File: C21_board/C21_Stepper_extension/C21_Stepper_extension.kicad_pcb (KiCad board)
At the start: 2 copper layers, 65.8 x 36.2 mm, 22 parts, among them J1 Conn_01x04_Male, J10 Conn_01x02_Male, J11 Conn_01x02_Male, J12 Conn_01x04_Male, J2 Conn_01x02_Male, J3 Conn_01x02_Male, J4 Conn_01x02_Male, J5 Jack-DC, J6 Screw_Terminal_01x02, J7 Conn_01x04_Male, J8 Conn_01x02_Male, J9 Conn_01x04_Male

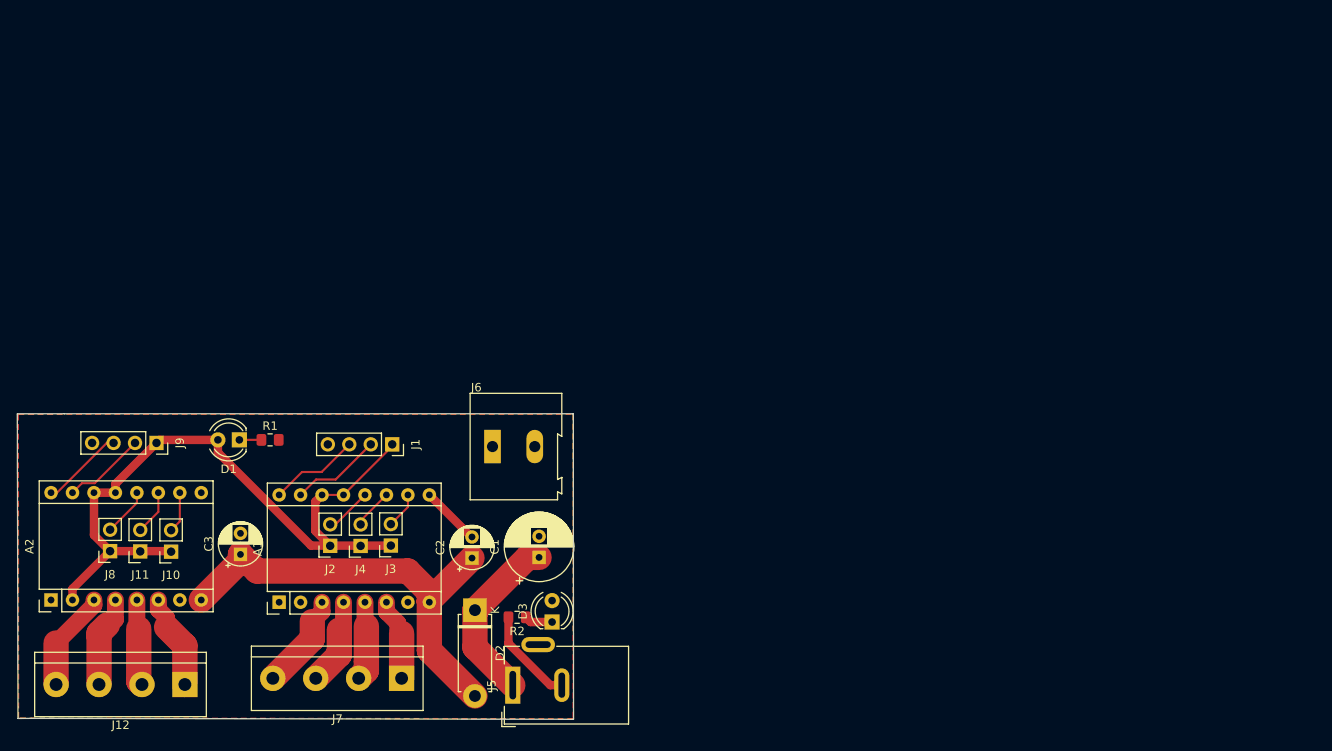
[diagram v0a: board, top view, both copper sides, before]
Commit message: add robot arm
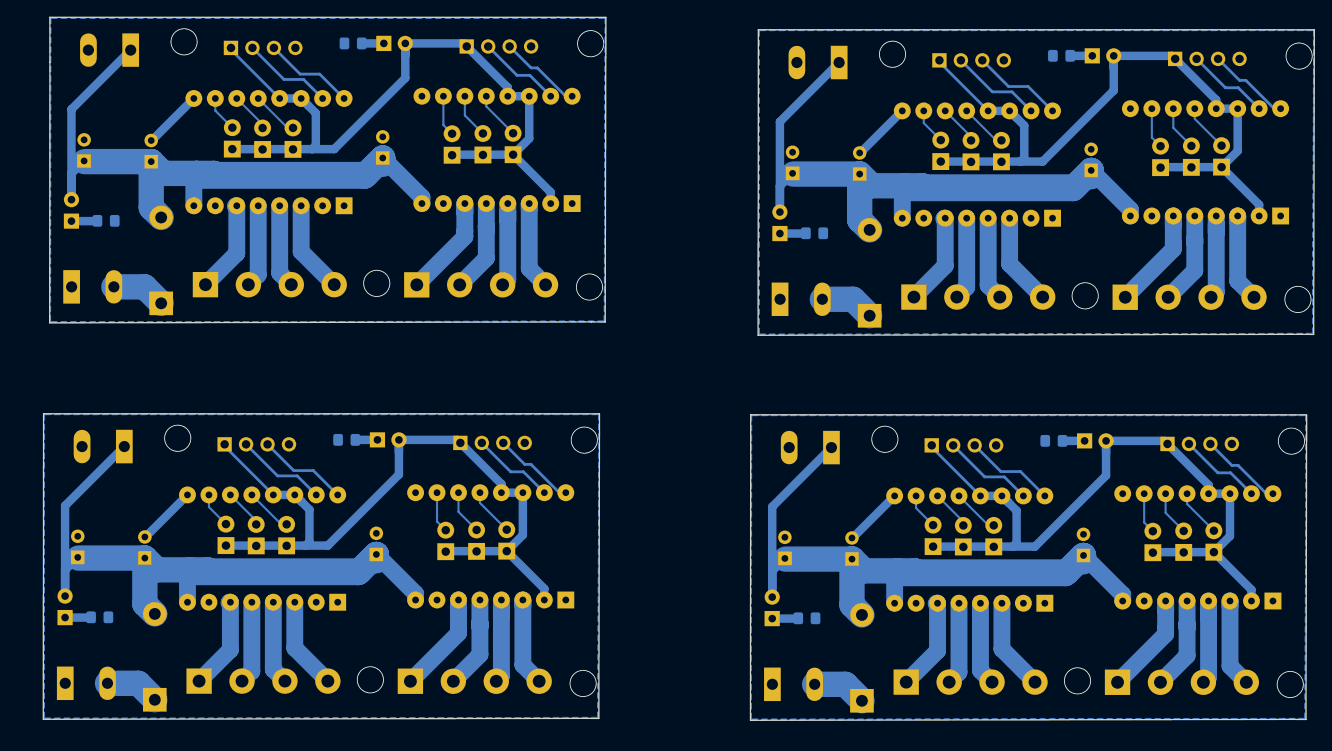
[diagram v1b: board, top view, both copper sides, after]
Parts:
- removed the J5 at (150.4, 103.6)
- added A1: Pololu_Breakout_DRV8825, drone_v3:Pololu_Breakout-16_15.2x20.3mm, B.Cu at (214.3, 48.4)
- added A1: Pololu_Breakout_DRV8825, drone_v3:Pololu_Breakout-16_15.2x20.3mm, B.Cu at (130.4, 46.9)
- added A1: Pololu_Breakout_DRV8825, drone_v3:Pololu_Breakout-16_15.2x20.3mm, B.Cu at (213.3, 93.9)
- added A2: Pololu_Breakout_DRV8825, Module:Pololu_Breakout-16_15.2x20.3mm, B.Cu at (240.3, 93.7)
- added A2: Pololu_Breakout_DRV8825, Module:Pololu_Breakout-16_15.2x20.3mm, B.Cu at (157.4, 46.6)
- added A2: Pololu_Breakout_DRV8825, Module:Pololu_Breakout-16_15.2x20.3mm, B.Cu at (241.3, 48.1)
- added C1: CP, Capacitor_THT:CP_Radial_D8.0mm_P2.50mm, B.Cu at (182.6, 88.6)
- added C1: CP, Capacitor_THT:CP_Radial_D8.0mm_P2.50mm, B.Cu at (183.5, 43.1)
- added C1: CP, Capacitor_THT:CP_Radial_D8.0mm_P2.50mm, B.Cu at (99.6, 41.6)
- added C2: CP, Capacitor_THT:CP_Radial_D5.0mm_P2.50mm, B.Cu at (190.5, 88.7)
- added C2: CP, Capacitor_THT:CP_Radial_D5.0mm_P2.50mm, B.Cu at (191.4, 43.1)
- added C2: CP, Capacitor_THT:CP_Radial_D5.0mm_P2.50mm, B.Cu at (107.6, 41.7)
- added C3: CP, Capacitor_THT:CP_Radial_D5.0mm_P2.50mm, B.Cu at (135.0, 41.2)
- added C3: CP, Capacitor_THT:CP_Radial_D5.0mm_P2.50mm, B.Cu at (217.9, 88.3)
- added C3: CP, Capacitor_THT:CP_Radial_D5.0mm_P2.50mm, B.Cu at (218.8, 42.7)
- added D1: LED, LED_THT:LED_D4.0mm, B.Cu at (135.1, 27.7)
- added D1: LED, LED_THT:LED_D4.0mm, B.Cu at (218.1, 74.7)
- added D1: LED, LED_THT:LED_D4.0mm, B.Cu at (219.0, 29.2)
- added D2: DIODE, Diode_THT:D_5W_P10.16mm_Horizontal, B.Cu at (191.7, 105.5)
- added D2: DIODE, Diode_THT:D_5W_P10.16mm_Horizontal, B.Cu at (108.8, 58.5)
- added D2: DIODE, Diode_THT:D_5W_P10.16mm_Horizontal, B.Cu at (192.6, 59.9)
- added D3: LED, LED_THT:LED_D4.0mm, B.Cu at (182.0, 50.2)
- added D3: LED, LED_THT:LED_D4.0mm, B.Cu at (98.1, 48.7)
- added D3: LED, LED_THT:LED_D4.0mm, B.Cu at (181.1, 95.8)
- added J1: Conn_01x04_Male, Connector_PinSocket_2.54mm:PinSocket_1x04_P2.54mm_Vertical, B.Cu at (200.0, 75.3)
- added J1: Conn_01x04_Male, Connector_PinSocket_2.54mm:PinSocket_1x04_P2.54mm_Vertical, B.Cu at (117.0, 28.2)
- added J1: Conn_01x04_Male, Connector_PinSocket_2.54mm:PinSocket_1x04_P2.54mm_Vertical, B.Cu at (200.9, 29.7)
- added J10: Conn_01x02_Male, drone_v3:PinSocket_1x02_P2.54mm_Vertical, B.Cu at (143.2, 40.9)
- added J10: Conn_01x02_Male, drone_v3:PinSocket_1x02_P2.54mm_Vertical, B.Cu at (226.1, 88.0)
- added J10: Conn_01x02_Male, drone_v3:PinSocket_1x02_P2.54mm_Vertical, B.Cu at (227.0, 42.4)
- added J11: Conn_01x02_Male, drone_v3:PinSocket_1x02_P2.54mm_Vertical, B.Cu at (146.8, 40.9)
- added J11: Conn_01x02_Male, drone_v3:PinSocket_1x02_P2.54mm_Vertical, B.Cu at (230.7, 42.4)
- added J11: Conn_01x02_Male, drone_v3:PinSocket_1x02_P2.54mm_Vertical, B.Cu at (229.8, 87.9)
- added J12: Conn_01x04_Male, TerminalBlock:TerminalBlock_bornier-4_P5.08mm, B.Cu at (222.9, 57.7)
- added J12: Conn_01x04_Male, TerminalBlock:TerminalBlock_bornier-4_P5.08mm, B.Cu at (139.0, 56.3)
- added J12: Conn_01x04_Male, TerminalBlock:TerminalBlock_bornier-4_P5.08mm, B.Cu at (222.0, 103.3)
- added J2: Conn_01x02_Male, Connector_PinSocket_2.54mm:PinSocket_1x02_P2.54mm_Vertical, B.Cu at (208.2, 41.7)
- added J2: Conn_01x02_Male, Connector_PinSocket_2.54mm:PinSocket_1x02_P2.54mm_Vertical, B.Cu at (207.3, 87.3)
- added J2: Conn_01x02_Male, Connector_PinSocket_2.54mm:PinSocket_1x02_P2.54mm_Vertical, B.Cu at (124.4, 40.2)
- added J3: Conn_01x02_Male, drone_v3:PinSocket_1x02_P2.54mm_Vertical, B.Cu at (201.0, 41.7)
- added J3: Conn_01x02_Male, drone_v3:PinSocket_1x02_P2.54mm_Vertical, B.Cu at (200.1, 87.2)
- added J3: Conn_01x02_Male, drone_v3:PinSocket_1x02_P2.54mm_Vertical, B.Cu at (117.2, 40.2)
- added J4: Conn_01x02_Male, drone_v3:PinSocket_1x02_P2.54mm_Vertical, B.Cu at (203.7, 87.3)
- added J4: Conn_01x02_Male, drone_v3:PinSocket_1x02_P2.54mm_Vertical, B.Cu at (204.6, 41.7)
- added J4: Conn_01x02_Male, drone_v3:PinSocket_1x02_P2.54mm_Vertical, B.Cu at (120.8, 40.2)
- added J5: Screw_Terminal_01x02, TerminalBlock:TerminalBlock_Altech_AK300-2_P5.00mm, B.Cu at (97.4, 103.4)
- added J5: Screw_Terminal_01x02, TerminalBlock:TerminalBlock_Altech_AK300-2_P5.00mm, B.Cu at (182.0, 58.0)
- added J5: Screw_Terminal_01x02, TerminalBlock:TerminalBlock_Altech_AK300-2_P5.00mm, B.Cu at (181.1, 103.5)
- added J5: Screw_Terminal_01x02, TerminalBlock:TerminalBlock_Altech_AK300-2_P5.00mm, B.Cu at (98.2, 56.5)
- added J6: Screw_Terminal_01x02, TerminalBlock:TerminalBlock_Altech_AK300-2_P5.00mm, B.Cu at (189.0, 29.9)
- added J6: Screw_Terminal_01x02, TerminalBlock:TerminalBlock_Altech_AK300-2_P5.00mm, B.Cu at (188.1, 75.5)
- added J6: Screw_Terminal_01x02, TerminalBlock:TerminalBlock_Altech_AK300-2_P5.00mm, B.Cu at (105.2, 28.5)
- added J7: Conn_01x04_Male, TerminalBlock:TerminalBlock_bornier-4_P5.08mm, B.Cu at (197.9, 57.7)
- added J7: Conn_01x04_Male, TerminalBlock:TerminalBlock_bornier-4_P5.08mm, B.Cu at (114.0, 56.2)
- added J7: Conn_01x04_Male, TerminalBlock:TerminalBlock_bornier-4_P5.08mm, B.Cu at (196.9, 103.3)
- added J8: Conn_01x02_Male, drone_v3:PinSocket_1x02_P2.54mm_Vertical, B.Cu at (150.4, 40.9)
- added J8: Conn_01x02_Male, drone_v3:PinSocket_1x02_P2.54mm_Vertical, B.Cu at (234.3, 42.3)
- added J8: Conn_01x02_Male, drone_v3:PinSocket_1x02_P2.54mm_Vertical, B.Cu at (233.4, 87.9)
- added J9: Conn_01x04_Male, Connector_PinSocket_2.54mm:PinSocket_1x04_P2.54mm_Vertical, B.Cu at (227.9, 75.1)
- added J9: Conn_01x04_Male, Connector_PinSocket_2.54mm:PinSocket_1x04_P2.54mm_Vertical, B.Cu at (228.8, 29.5)
- added J9: Conn_01x04_Male, Connector_PinSocket_2.54mm:PinSocket_1x04_P2.54mm_Vertical, B.Cu at (144.9, 28.1)
- added R1: R, Resistor_SMD:R_0805_2012Metric_Pad1.15x1.40mm_HandSolder, B.Cu at (131.5, 27.7)
- added R1: R, Resistor_SMD:R_0805_2012Metric_Pad1.15x1.40mm_HandSolder, B.Cu at (215.3, 29.2)
- added R1: R, Resistor_SMD:R_0805_2012Metric_Pad1.15x1.40mm_HandSolder, B.Cu at (214.4, 74.7)
- added R2: R, Resistor_SMD:R_0805_2012Metric_Pad1.15x1.40mm_HandSolder, B.Cu at (102.2, 48.7)
- added R2: R, Resistor_SMD:R_0805_2012Metric_Pad1.15x1.40mm_HandSolder, B.Cu at (185.2, 95.7)
- added R2: R, Resistor_SMD:R_0805_2012Metric_Pad1.15x1.40mm_HandSolder, B.Cu at (186.1, 50.2)
- A1: footprint Module:Pololu_Breakout-16_15.2x20.3mm -> drone_v3:Pololu_Breakout-16_15.2x20.3mm; moved to B.Cu
- A2, C1, C2, C3, D1, D2, D3, J1, J12, J2, J6, J7, J9, R1, R2: moved to B.Cu
- J10, J11, J3, J4, J8: footprint Connector_PinSocket_2.54mm:PinSocket_1x02_P2.54mm_Vertical -> drone_v3:PinSocket_1x02_P2.54mm_Vertical; moved to B.Cu
- moved A2 60.9 mm to (156.7, 93.6)
- moved D3 57.6 mm to (97.4, 95.6)
- moved C1 54.6 mm to (98.9, 88.5)
- moved R2 49.4 mm to (101.5, 95.6), turned to 0 degrees
- moved J8 46.9 mm to (149.7, 87.8), turned to 0 degrees
- moved J6 43.6 mm to (104.4, 75.4), turned to 180 degrees
- moved J11 39.8 mm to (146.1, 87.8), turned to 0 degrees
- moved D2 39.3 mm to (108.0, 105.4), turned to 90 degrees
- moved C2 38.7 mm to (106.8, 88.6)
- moved J9 36.0 mm to (144.2, 75.0)
- moved J10 32.5 mm to (142.4, 87.8), turned to 0 degrees
- moved J12 26.7 mm to (138.3, 103.2), turned to 0 degrees
- moved J7 24.0 mm to (113.3, 103.2), turned to 0 degrees
- moved J1 19.8 mm to (116.3, 75.1)
- moved J3 19.5 mm to (116.4, 87.1), turned to 0 degrees
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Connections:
- A1 pad 8: Net-(A1-Pad8) -> +12V
- A2 pad 8: Net-(A1-Pad8) -> +12V
- C2 pad 1: Net-(A1-Pad8) -> +12V
- C3 pad 1: Net-(A1-Pad8) -> +12V
- D2 pad 1: +12V -> Net-(D2-Pad1)
- D2 pad 2: Net-(A1-Pad8) -> +12V
- D3 pad 2: Net-(A1-Pad8) -> +12V
- J6 pad 1: Net-(A1-Pad8) -> +12V
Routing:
- net +12V: track 21.1 -> 428.1 mm
- net +3V3: track 92.2 -> 384.5 mm
- net Net-(A1-Pad8): track 53.3 -> 0.00 mm
- net Net-(A2-Pad6): track 11.3 -> 52.4 mm
- net Net-(A2-Pad5): track 10.2 -> 45.8 mm
- net Net-(A1-Pad6): track 9.75 -> 44.2 mm
- net Net-(A2-Pad4): track 17.3 -> 51.7 mm
- net Net-(A1-Pad3): track 11.4 -> 43.8 mm
- net Net-(A2-Pad16): track 9.84 -> 42.2 mm
- net Net-(A1-Pad15): track 10.8 -> 43.1 mm
- net Net-(A1-Pad16): track 10.8 -> 43.1 mm
- net Net-(A2-Pad3): track 11.9 -> 44.1 mm
- net Net-(A1-Pad5): track 9.45 -> 39.3 mm
- net Net-(A2-Pad15): track 9.84 -> 39.4 mm
- net Net-(A1-Pad4): track 10.4 -> 39.6 mm
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- added copper zone on B.Cu, net GND
- removed copper zone on F.Cu, net GND
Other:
- board size 65.8 x 36.2 mm -> 150.4 x 83.2 mm
